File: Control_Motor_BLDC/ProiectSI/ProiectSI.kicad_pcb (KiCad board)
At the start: 2 copper layers, 88 x 126.5 mm, 65 parts, among them J1 Screw_Terminal_01x05, J2 Conn_01x04_Pin, J3 Screw_Terminal_01x03, J5 Conn_01x02_Pin, SW1 SW_Nidec_CAS-120A1, U1 STSPIN32F0A, U2 DRV5055A2xDBZxQ1, U3 DRV5055A2xDBZxQ1, U4 DM-OLED096-636

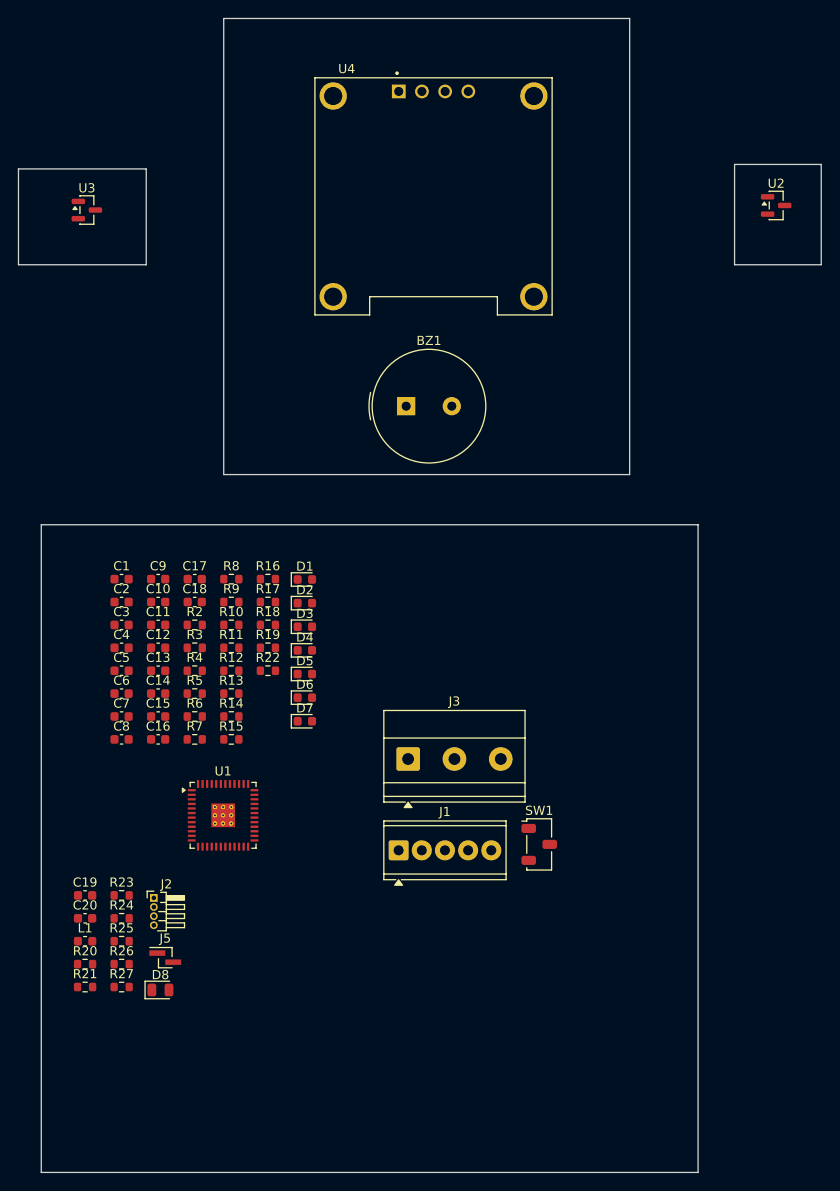
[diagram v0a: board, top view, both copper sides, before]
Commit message: Realizat layout PCB
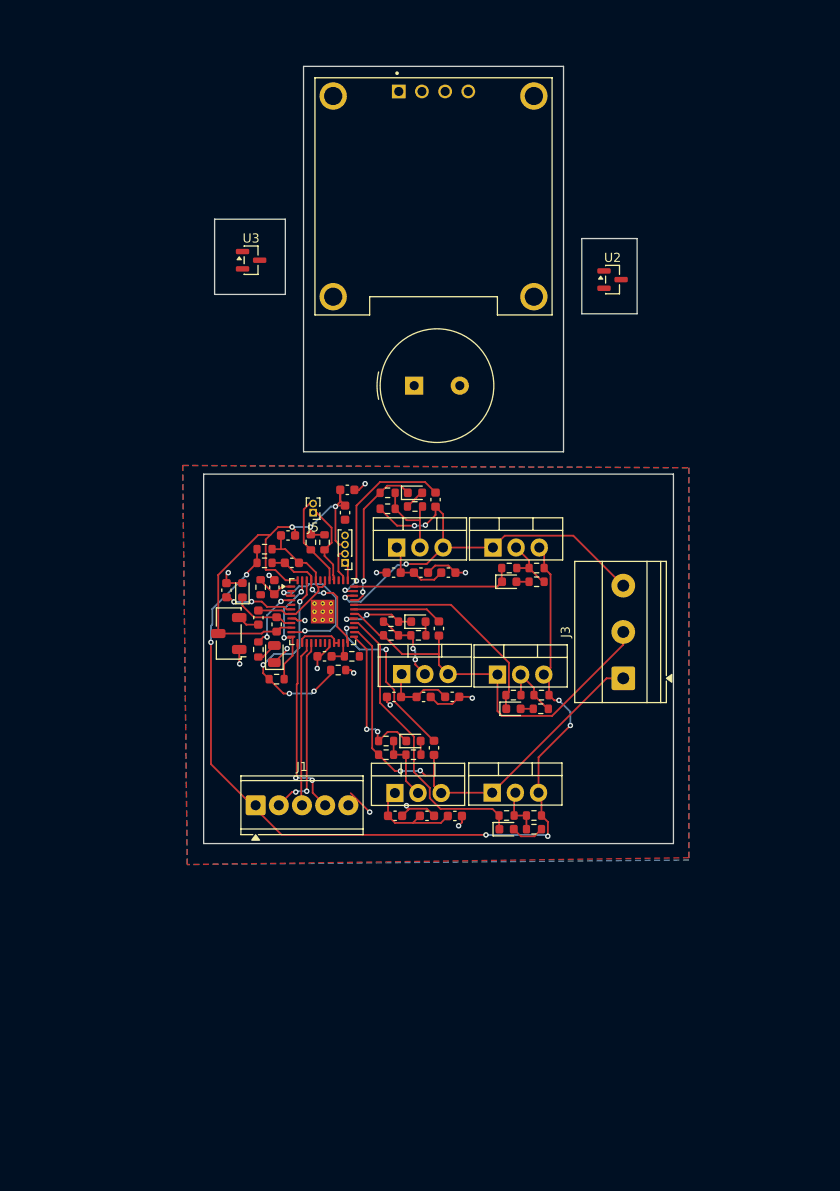
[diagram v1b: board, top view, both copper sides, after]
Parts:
- added Q1: NMOS_Substrate, Package_TO_SOT_THT:TO-220-3_Vertical, F.Cu at (158.0, 88.0)
- added Q2: NMOS_Substrate, Package_TO_SOT_THT:TO-220-3_Vertical, F.Cu at (168.5, 88.0)
- added Q3: NMOS_Substrate, Package_TO_SOT_THT:TO-220-3_Vertical, F.Cu at (158.5, 101.9)
- added Q4: NMOS_Substrate, Package_TO_SOT_THT:TO-220-3_Vertical, F.Cu at (169.0, 101.9)
- added Q5: NMOS_Substrate, Package_TO_SOT_THT:TO-220-3_Vertical, F.Cu at (157.8, 114.9)
- added Q6: NMOS_Substrate, Package_TO_SOT_THT:TO-220-3_Vertical, F.Cu at (168.4, 114.9)
- added R1: 0.01, Resistor_SMD:R_0603_1608Metric, F.Cu at (143.5, 88.2)
- J2: footprint Connector_PinHeader_1.00mm:PinHeader_1x04_P1.00mm_Horizontal -> Connector_PinHeader_1.00mm:PinHeader_1x04_P1.00mm_Vertical
- J5: footprint Connector_PinHeader_1.00mm:PinHeader_1x02_P1.00mm_Vertical_SMD_Pin1Left -> Connector_PinHeader_1.00mm:PinHeader_1x02_P1.00mm_Vertical
- moved R27 53.6 mm to (150.0, 87.4), turned to -90 degrees
- moved J5 51.4 mm to (148.8, 84.2), turned to 180 degrees
- moved R26 50.7 mm to (148.5, 87.4), turned to -90 degrees
- moved R21 47.9 mm to (143.0, 92.3), turned to 90 degrees
- moved R20 44.7 mm to (153.0, 99.9), turned to 180 degrees
- moved J2 42.3 mm to (152.3, 89.7), turned to 180 degrees
- moved C20 41.8 mm to (144.5, 92.3), turned to 90 degrees
- moved SW1 41.1 mm to (139.5, 97.4), turned to 180 degrees
- moved L1 40.6 mm to (144.8, 96.4), turned to -90 degrees
- moved C8 40.2 mm to (163.6, 90.7)
- moved R5 39.4 mm to (173.3, 91.7), turned to 180 degrees
- moved R4 39.1 mm to (173.3, 90.2)
- moved D8 38.9 mm to (144.5, 99.7), turned to 90 degrees
- moved R11 38.7 mm to (173.0, 118.9)
- moved R7 38.1 mm to (173.8, 105.7), turned to 180 degrees
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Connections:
- J5 pad 2: SDA -> SDCLK
- R26 pad 2: SDA -> SDCLK
- U1 pad 41: SDA -> SDCLK
- U4 pad 3: SDA -> SDCLK
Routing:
- net Net-(Q2-Bulk): track 0.00 -> 101.7 mm, vias 0 -> 6
- net VDD: track 0.00 -> 52.2 mm, vias 0 -> 3
- net OutW: track 0.00 -> 51.5 mm, vias 0 -> 2
- net RshuntNeg: track 0.00 -> 50.4 mm, vias 0 -> 13
- net OutU: track 0.00 -> 50.1 mm, vias 0 -> 4
- net OutV: track 0.00 -> 43.8 mm
- net LW: track 0.00 -> 32.8 mm
- net Vm: track 0.00 -> 31.7 mm, vias 0 -> 2
- net LV: track 0.00 -> 24.8 mm
- net Net-(U1-OP3N): track 0.00 -> 23.1 mm, vias 0 -> 4
- net VbootU: track 0.00 -> 21.2 mm, vias 0 -> 2
- net HallW: track 0.00 -> 20.2 mm, vias 0 -> 2
- net HallU: track 0.00 -> 20.1 mm, vias 0 -> 2
- net VbootW: track 0.00 -> 18.9 mm, vias 0 -> 2
- net HallV: track 0.00 -> 18.1 mm
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- added copper zone on B.Cu, net RshuntNeg
- added copper zone on F.Cu, net RshuntNeg
- added copper zone on In1.Cu, net RshuntNeg
- added copper zone on In2.Cu, net Vm
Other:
- board size 88 x 126.5 mm -> 51.5 x 85.2 mm
- copper layers 2 -> 4

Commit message: Modificare proiecte
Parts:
- removed BZ1: Buzzer, Buzzer_Beeper:Buzzer_TDK_PS1240P02BT_D12.2mm_H6.5mm
- removed D8: LED, LED_SMD:LED_0805_2012Metric
- removed Q1, Q2, Q3, Q4, Q5, Q6: NMOS_Substrate, Package_TO_SOT_THT:TO-220-3_Vertical
- removed R25: 130, Resistor_SMD:R_0603_1608Metric
- added BZ2: Buzzer, Buzzer_Beeper:Buzzer_TDK_PS1240P02BT_D12.2mm_H6.5mm, F.Cu at (159.6, 70.2)
- added C20: 100nF, Capacitor_SMD:C_0603_1608Metric, F.Cu at (163.4, 102.9)
- added C21: 1u, Capacitor_SMD:C_0603_1608Metric, F.Cu at (144.8, 121.0)
- added C22: 1u, Capacitor_SMD:C_0603_1608Metric, F.Cu at (138.2, 119.3)
- added C23: 100nF, Capacitor_SMD:C_0603_1608Metric, F.Cu at (172.2, 102.9)
- added D9: LED, LED_SMD:LED_0805_2012Metric, F.Cu at (139.0, 116.5)
- added Maneta_Accel1: Conn_01x03, Connector_PinHeader_2.54mm:PinHeader_1x03_P2.54mm_Vertical, F.Cu at (182.1, 121.2)
- added Maneta_Frana1: Conn_01x03, Connector_PinHeader_2.54mm:PinHeader_1x03_P2.54mm_Vertical, F.Cu at (186.7, 121.2)
- added Q10: RD3L150SNTL1, RD3L150SNTL:RD3P175SNFRATL, F.Cu at (171.2, 94.2)
- added Q11: RD3L150SNTL1, RD3L150SNTL:RD3P175SNFRATL, F.Cu at (170.8, 110.7)
- added Q12: RD3L150SNTL1, RD3L150SNTL:RD3P175SNFRATL, F.Cu at (170.8, 125.2)
- added Q13: BC846B, BC846B:SOT95P230X110-3N, F.Cu at (135.1, 115.6)
- added Q14: BC846B, BC846B:SOT95P230X110-3N, F.Cu at (145.4, 115.8)
- added Q7: RD3L150SNTL1, RD3L150SNTL:RD3P175SNFRATL, F.Cu at (156.8, 94.3)
- added Q8: RD3L150SNTL1, RD3L150SNTL:RD3P175SNFRATL, F.Cu at (156.8, 110.8)
- added Q9: RD3L150SNTL1, RD3L150SNTL:RD3P175SNFRATL, F.Cu at (156.8, 125.3)
- added R20: 1k, Resistor_SMD:R_0603_1608Metric, F.Cu at (168.9, 102.9)
- added R21: 1k, Resistor_SMD:R_0603_1608Metric, F.Cu at (160.0, 102.9)
- added R28: 10k, Resistor_SMD:R_0603_1608Metric, F.Cu at (134.7, 112.7)
- added R30: 10k, Resistor_SMD:R_0603_1608Metric, F.Cu at (144.7, 118.9)
- added R_sig1: 100k, Resistor_SMD:R_0603_1608Metric, F.Cu at (172.2, 105.4)
- added R_sig2: 100k, Resistor_SMD:R_0603_1608Metric, F.Cu at (163.4, 105.4)
- R23: value 30k -> 21k
- R24: value 1k -> 1.43k
- moved C13 14.9 mm to (158.8, 131.2)
- moved C12 14.9 mm to (152.3, 131.2)
- moved C14 14.9 mm to (155.8, 131.2)
- moved D5 14.0 mm to (165.0, 132.0)
- moved R10 14.0 mm to (165.0, 130.5)
- moved R11 14.0 mm to (168.0, 132.0)
- moved R17 14.0 mm to (168.0, 130.5)
- moved D2 13.6 mm to (165.0, 118.0)
- moved R6 13.6 mm to (165.0, 116.5)
- moved R7 13.6 mm to (168.0, 118.0)
- moved R16 13.6 mm to (168.0, 116.5)
- moved C11 13.2 mm to (155.0, 116.1)
- moved C9 13.2 mm to (151.7, 116.1)
- moved C10 13.2 mm to (158.1, 116.1)
- moved R24 11.7 mm to (145.6, 111.5)
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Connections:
- R10 pad 1: Net-(Q6-G) -> Net-(D5-A)
- R12 pad 2: Net-(Q5-G) -> Net-(D6-A)
- R14 pad 1: Net-(Q1-G) -> Net-(D1-A)
- R15 pad 1: Net-(Q3-G) -> Net-(D4-A)
- R16 pad 1: Net-(Q4-G) -> Net-(D2-A)
- R17 pad 1: Net-(Q6-G) -> Net-(D5-A)
- R18 pad 1: Net-(Q5-G) -> Net-(D6-A)
- R22 pad 1: Net-(Q2-G) -> Net-(D3-A)
- R3 pad 2: Net-(Q1-G) -> Net-(D1-A)
- R4 pad 1: Net-(Q2-G) -> Net-(D3-A)
- R6 pad 1: Net-(Q4-G) -> Net-(D2-A)
- R8 pad 2: Net-(Q3-G) -> Net-(D4-A)
- SW1 pad 1: RshuntNeg -> Net-(SW1-C)
- U1 pad 4: Net-(U1-PF0) -> Led_control
- U1 pad 5: Net-(BZ1-+) -> Buzer_control
- U1 pad 7: RshuntNeg -> Net-(SW1-C)
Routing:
- net RshuntNeg: track 50.4 -> 178.3 mm, vias 13 -> 19
- net VDD: track 52.2 -> 130.8 mm, vias 3 -> 7
- net Accel: track 2.91 -> 67.2 mm, vias 0 -> 2
- net Net-(Q10-S): track 101.7 -> 150.2 mm, vias 6 -> 4
- net Net-(Maneta_Frana1-Pin_2): track 0.00 -> 40.1 mm, vias 0 -> 2
- net Frana: track 4.44 -> 36.4 mm, vias 0 -> 2
- net OutU: track 50.1 -> 78.0 mm
- net Net-(Maneta_Accel1-Pin_2): track 0.00 -> 27.3 mm, vias 0 -> 2
- net Buzer_control: track 0.00 -> 24.3 mm, vias 0 -> 2
- net Vm: track 31.7 -> 50.9 mm, vias 2 -> 4
- net Net-(D6-A): track 1.52 -> 19.9 mm, vias 0 -> 2
- net Net-(D1-A): track 2.23 -> 19.4 mm
- net Net-(D4-A): track 1.52 -> 18.4 mm, vias 0 -> 2
- net Net-(D3-A): track 1.39 -> 14.6 mm
- net Led_control: track 0.00 -> 12.6 mm, vias 0 -> 2
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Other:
- board size 51.5 x 85.2 mm -> 59 x 99.2 mm
